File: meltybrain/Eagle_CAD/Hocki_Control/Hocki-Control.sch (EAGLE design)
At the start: 123 parts, among them J1 SM03B-SRSS-TB(LF)(SN), J2 SM03B-SRSS-TB(LF)(SN), J3 SM03B-SRSS-TB(LF)(SN), J4 SM04B-SRSS-TB(LF)(SN), J5 SM04B-SRSS-TB(LF)(SN), U1 TEENSY_4.1, U10 TLV3502AIDCNR, U11 NL27WZ32USG, U12 NL27WZ32USG, U13 HMC1052L-TR, U14 LMV358, U15 IRF7509, U16 TMUX1219DCKR, U17 LMV358, U18 LMV358, U19 AP2210K-3.3TRG1, U2 ADXL375, U20 AP2210K-5.0TRG1, U21 AP63200, U22 74AHC1G04GW,125, U23 LDL212PU50R, U3 ADXL375, U4 ADXL375, U5 ADXL375, U6 LMH6612MAX/NOPB, U7 LMH6612MAX/NOPB, U8 LMH6612MAX/NOPB, U9 LMH6612MAX/NOPB

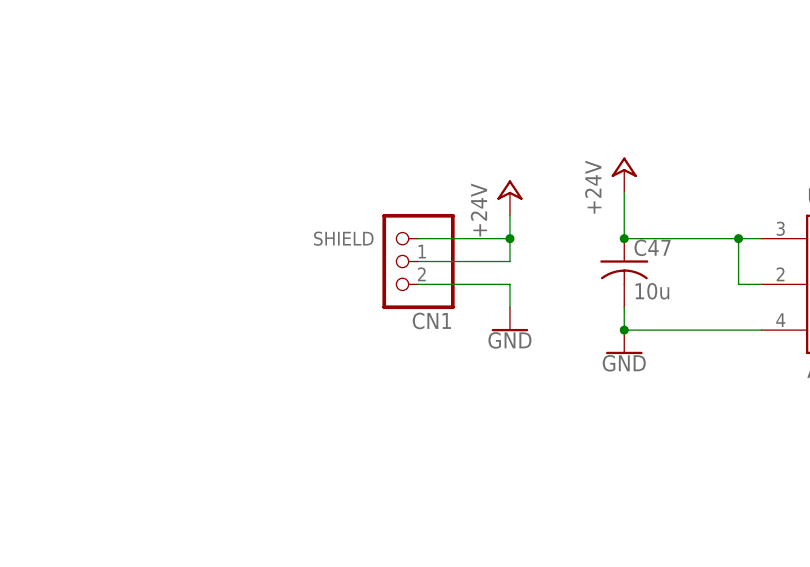
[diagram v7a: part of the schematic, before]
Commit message: Added 3d models, replaced power connetor, added photo
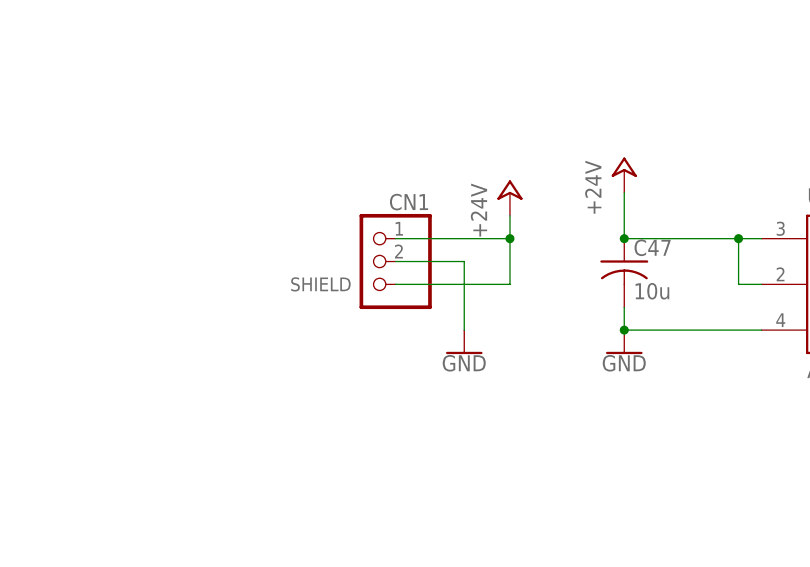
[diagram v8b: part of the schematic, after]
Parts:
- CN1: device Hocki_Library:JST_2PIN-SMT-RA -> Hocki_Library:JST_2PIN
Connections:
- net +24V: now also CN1.1; no longer CN1.2
- net GND: now also CN1.2; no longer CN1.1
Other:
- moved on the sheet: CN1
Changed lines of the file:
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@@
 <?xml version="1.0" encoding="utf-8"?>
 <!DOCTYPE eagle SYSTEM "eagle.dtd">
-<eagle version="9.5.2">
+<eagle version="9.6.2">
 <drawing>
 <settings>
@@
 <setting verticaltext="up"/>
 </settings>
-<grid distance="0.1" unitdist="inch" unit="inch" style="lines" multiple="1" display="yes" altdistance="0.01" altunitdist="inch" altunit="inch"/>
+<grid distance="0.1" unitdist="inch" unit="inch" style="lines" multiple="1" display="no" altdistance="0.01" altunitdist="inch" altunit="inch"/>
 <layers>
 <layer number="1" name="Top" color="4" fill="1" visible="no" active="no"/>
@@
 </classes>
 <parts>
-<part name="U1" library="Hocki_Library" deviceset="TEENSY_4.1" device=""/>
+<part name="U1" library="Hocki_Library" deviceset="TEENSY_4.1" device="" override_package3d_urn="urn:adsk.eagle:package:22261832/3" override_package_urn="urn:adsk.eagle:footprint:22261835/1"/>
 <part name="U2" library="Hocki_Library" deviceset="ADXL375" device=""/>
 <part name="SUPPLY1" library="SparkFun-PowerSymbols" library_urn="urn:adsk.eagle:library:530" deviceset="3.3V" device=""/>
@@
 <part name="GND59" library="SparkFun-PowerSymbols" library_urn="urn:adsk.eagle:library:530" deviceset="GND" device=""/>
 <part name="SUPPLY22" library="Hocki_Library" deviceset="9V" device=""/>
-<part name="J3" library="Hocki_Library" deviceset="SM03B-SRSS-TB(LF)(SN)" device=""/>
+<part name="J3" library="Hocki_Library" deviceset="SM03B-SRSS-TB(LF)(SN)" device="" override_package3d_urn="urn:adsk.eagle:package:22261818/2" override_package_urn="urn:adsk.eagle:footprint:22261819/1"/>
 <part name="GND60" library="SparkFun-PowerSymbols" library_urn="urn:adsk.eagle:library:530" deviceset="GND" device=""/>
 <part name="SUPPLY23" library="SparkFun-PowerSymbols" library_urn="urn:adsk.eagle:library:530" deviceset="5V" device=""/>
@@
 <part name="GND57" library="SparkFun-PowerSymbols" library_urn="urn:adsk.eagle:library:530" deviceset="GND" device=""/>
 <part name="L1" library="Hocki_Library" deviceset="LQH5BPN100M38L" device="" value="10uH"/>
-<part name="J4" library="Hocki_Library" deviceset="SM04B-SRSS-TB(LF)(SN)" device=""/>
+<part name="J4" library="Hocki_Library" deviceset="SM04B-SRSS-TB(LF)(SN)" device="" override_package3d_urn="urn:adsk.eagle:package:22261809/2" override_package_urn="urn:adsk.eagle:footprint:22261810/1"/>
 <part name="J5" library="Hocki_Library" deviceset="SM04B-SRSS-TB(LF)(SN)" device=""/>
 <part name="P+2" library="supply1" library_urn="urn:adsk.eagle:library:371" deviceset="+5V" device=""/>
@@
 <part name="P+5" library="supply1" library_urn="urn:adsk.eagle:library:371" deviceset="+24V" device=""/>
 <part name="GND67" library="SparkFun-PowerSymbols" library_urn="urn:adsk.eagle:library:530" deviceset="GND" device=""/>
-<part name="CN1" library="Hocki_Library" deviceset="JST_2PIN" device="-SMT-RA"/>
+<part name="CN1" library="Hocki_Library" deviceset="JST_2PIN" device="" override_package3d_urn="urn:adsk.eagle:package:22261884/2" override_package_urn="urn:adsk.eagle:footprint:6240117/1"/>
 </parts>
 <sheets>
@@
 <attribute name="VALUE" x="134.62" y="50.8" size="1.778" layer="96" rot="R90"/>
 </instance>
-<instance part="GND67" gate="1" x="137.16" y="40.64" smashed="yes">
-<attribute name="VALUE" x="137.16" y="40.386" size="1.778" layer="96" align="top-center"/>
+<instance part="GND67" gate="1" x="132.08" y="38.1" smashed="yes">
+<attribute name="VALUE" x="132.08" y="37.846" size="1.778" layer="96" align="top-center"/>
 </instance>
-<instance part="CN1" gate="G$1" x="124.46" y="48.26" smashed="yes" rot="R180">
-<attribute name="NAME" x="130.81" y="42.545" size="1.778" layer="95" rot="R180"/>
-<attribute name="VALUE" x="130.81" y="55.88" size="1.778" layer="96" rot="R180"/>
+<instance part="CN1" gate="G$1" x="121.92" y="48.26" smashed="yes" rot="MR0">
+<attribute name="NAME" x="128.27" y="53.975" size="1.778" layer="95" rot="MR0"/>
+<attribute name="VALUE" x="128.27" y="40.64" size="1.778" layer="96" rot="MR0"/>
 </instance>
 </instances>
@@
 </segment>
 <segment>
-<wire x1="137.16" y1="45.72" x2="137.16" y2="43.18" width="0.1524" layer="91"/>
+<pinref part="CN1" gate="G$1" pin="2"/>
+<wire x1="124.46" y1="48.26" x2="132.08" y2="48.26" width="0.1524" layer="91"/>
 <pinref part="GND67" gate="1" pin="GND"/>
-<pinref part="CN1" gate="G$1" pin="1"/>
-<wire x1="137.16" y1="45.72" x2="127" y2="45.72" width="0.1524" layer="91"/>
+<wire x1="132.08" y1="48.26" x2="132.08" y2="40.64" width="0.1524" layer="91"/>
 </segment>
 </net>
@@
 </segment>
 <segment>
-<wire x1="137.16" y1="48.26" x2="137.16" y2="50.8" width="0.1524" layer="91"/>
+<pinref part="CN1" gate="G$1" pin="SHIELD"/>
+<wire x1="124.46" y1="45.72" x2="137.16" y2="45.72" width="0.1524" layer="91"/>
 <pinref part="P+5" gate="1" pin="+24V"/>
-<pinref part="CN1" gate="G$1" pin="2"/>
+<wire x1="137.16" y1="45.72" x2="137.16" y2="50.8" width="0.1524" layer="91"/>
+<pinref part="CN1" gate="G$1" pin="1"/>
 <wire x1="137.16" y1="50.8" x2="137.16" y2="53.34" width="0.1524" layer="91"/>
-<wire x1="137.16" y1="48.26" x2="127" y2="48.26" width="0.1524" layer="91"/>
-<pinref part="CN1" gate="G$1" pin="SHIELD"/>
-<wire x1="127" y1="50.8" x2="137.16" y2="50.8" width="0.1524" layer="91"/>
+<wire x1="124.46" y1="50.8" x2="137.16" y2="50.8" width="0.1524" layer="91"/>
 <junction x="137.16" y="50.8"/>
 </segment>
@@
 packages will not be understood (or retained) with this version.
 </note>
+<note version="9.4" severity="warning">
+Since Version 9.4, EAGLE supports the overriding of 3D packages
+in schematics and board files. Those overridden 3d packages
+will not be understood (or retained) with this version.
+</note>
 <note version="8.4" severity="warning">
